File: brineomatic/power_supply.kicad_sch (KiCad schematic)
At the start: 26 parts, among them J8 5.08MM, J9 5.08MM, Q3 20N06, U2 LM74700, U3 XL1509-5.0

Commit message: silkscreen good and all drc errors fixed.
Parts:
- J9: footprint Connector_Phoenix_MSTB:PhoenixContact_MSTBA_2,5_2-G-5,08_1x02_P5.08mm_Horizontal -> yarrboard:PhoenixContact_MSTBA_2,5_2-G-5,08_1x02_P5.08mm_Horizontal
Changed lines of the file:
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@@
 			)
 		)
-		(property "Footprint" "Connector_Phoenix_MSTB:PhoenixContact_MSTBA_2,5_2-G-5,08_1x02_P5.08mm_Horizontal"
+		(property "Footprint" "yarrboard:PhoenixContact_MSTBA_2,5_2-G-5,08_1x02_P5.08mm_Horizontal"
 			(at 46.99 52.07 0)
 			(effects

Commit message: worked on bom for rev b prototype run
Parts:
- C10: value 4.7uF/50v -> 4.7uF / 50v; LCSC C437557 -> (none); now not fitted
- C11: value 10uF/35v -> 10uF / 35v
- C6: LCSC C83170 -> (none)
- C7, C9: LCSC C49678 -> (none)
- C8: value 470nF/50v -> 470nF / 50v; LCSC C106843 -> (none)
- D10, D8: value PWR -> RED; LCSC (none) -> C965799
- D6: LCSC (none) -> C151246
- D7: LCSC (none) -> C148225
- Q3: LCSC (none) -> C36499181
- R18: LCSC C137513 -> (none); now not fitted
- U2: LCSC (none) -> C2941042
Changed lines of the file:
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@@
 			)
 		)
-		(property "Value" "PWR"
+		(property "Value" "RED"
 			(at 143.51 57.4674 90)
 			(effects
@@
 		(property "Sim.Pins" "1=K 2=A"
 			(at 139.7 54.61 0)
+			(effects
+				(font
+					(size 1.27 1.27)
+				)
+				(hide yes)
+			)
+		)
+		(property "LCSC" "C965799"
+			(at 139.7 54.61 90)
 			(effects
 				(font
@@
 			)
 		)
+		(property "LCSC" "C2941042"
+			(at 115.57 62.23 0)
+			(effects
+				(font
+					(size 1.27 1.27)
+				)
+				(hide yes)
+			)
+		)
 		(pin "6"
 		)
@@
 		(in_bom yes)
 		(on_board yes)
-		(dnp no)
+		(dnp yes)
 		(fields_autoplaced yes)
 		(property "Reference" "R18"
@@
 			)
 		)
-		(property "LCSC" "C137513"
+		(property "LCSC" ""
 			(at 118.11 132.08 0)
 			(effects
@@
 			)
 		)
-		(property "LCSC" "C49678"
+		(property "LCSC" ""
 			(at 148.59 128.27 0)
 			(effects
@@
 			)
 		)
+		(property "LCSC" "C36499181"
+			(at 115.57 46.99 90)
+			(effects
+				(font
+					(size 1.27 1.27)
+				)
+				(hide yes)
+			)
+		)
 		(pin "1"
 		)
@@
 			)
 		)
+		(property "LCSC" "C148225"
+			(at 74.93 66.04 90)
+			(effects
+				(font
+					(size 1.27 1.27)
+				)
+				(hide yes)
+			)
+		)
 		(pin "1"
 		)
@@
 			)
 		)
-		(property "LCSC" "C49678"
+		(property "LCSC" ""
 			(at 96.52 58.42 0)
 			(effects
@@
 		(in_bom yes)
 		(on_board yes)
-		(dnp no)
+		(dnp yes)
 		(fields_autoplaced yes)
 		(property "Reference" "C10"
@@
 			)
 		)
-		(property "Value" "4.7uF/50v"
+		(property "Value" "4.7uF / 50v"
 			(at 120.65 125.7363 0)
 			(effects
@@
 			)
 		)
-		(property "LCSC" "C437557"
+		(property "LCSC" ""
 			(at 118.11 124.46 0)
 			(effects
@@
 			)
 		)
+		(property "LCSC" "C151246"
+			(at 74.93 58.42 90)
+			(effects
+				(font
+					(size 1.27 1.27)
+				)
+				(hide yes)
+			)
+		)
 		(pin "1"
 		)
@@
 			)
 		)
-		(property "Value" "PWR"
+		(property "Value" "RED"
 			(at 234.95 127.3174 90)
 			(effects
@@
 			)
 		)
+		(property "LCSC" "C965799"
+			(at 231.14 124.46 90)
+			(effects
+				(font
+					(size 1.27 1.27)
+				)
+				(hide yes)
+			)
+		)
 		(pin "1"
 		)
@@
 			)
 		)
-		(property "LCSC" "C83170"
+		(property "LCSC" ""
 			(at 72.39 128.27 0)
 			(effects
@@
 			)
 		)
-		(property "Value" "10uF/35v"
+		(property "Value" "10uF / 35v"
 			(at 134.62 129.5463 0)
 			(effects
@@
 			)
 		)
-		(property "Value" "470nF/50v"
+		(property "Value" "470nF / 50v"
 			(at 95.25 129.5463 0)
 			(effects
@@
 			)
 		)
-		(property "LCSC" "C106843"
+		(property "LCSC" ""
 			(at 92.71 128.27 0)
 			(effects

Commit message: updated jlc parts rotations and placement offsets
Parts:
- Q3: Position Offset (none) -> -1.778,0.0; Rotation Offset (none) -> 180
- U2: Rotation Offset (none) -> 90
- U3: Rotation Offset (none) -> 180
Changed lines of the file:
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@@
+			)
+		)
+		(property "Rotation Offset" "180"
+			(at 168.91 123.19 0)
+			(effects
+				(font
+					(size 1.27 1.27)
+				)
+				(hide yes)
 			)
 		)
@@
 		)
 		(property "LCSC" "C2941042"
+			(at 115.57 62.23 0)
+			(effects
+				(font
+					(size 1.27 1.27)
+				)
+				(hide yes)
+			)
+		)
+		(property "Rotation Offset" "90"
 			(at 115.57 62.23 0)
 			(effects
@@
 			(at 115.57 46.99 90)
 			(effects
+				(font
+					(size 1.27 1.27)
+				)
+				(hide yes)
+			)
+		)
+		(property "Rotation Offset" "180"
+			(at 115.57 46.99 90)
+			(effects
+				(font
+					(size 1.27 1.27)
+				)
+				(hide yes)
+			)
+		)
+		(property "Position Offset" "-1.778,0.0"
+			(at 115.57 46.99 90)
+			(effects

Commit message: added qwiic i2c connector
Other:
- title: (none) -> https://github.com/hoeken/brineomatic
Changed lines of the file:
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@@
 	(generator_version "9.0")
 	(paper "A4")
+	(title_block
+		(title "https://github.com/hoeken/brineomatic")
+		(date "2025-08-28")
+		(rev "B")
+	)
 	(rectangle
 		(start 21.59 21.59)

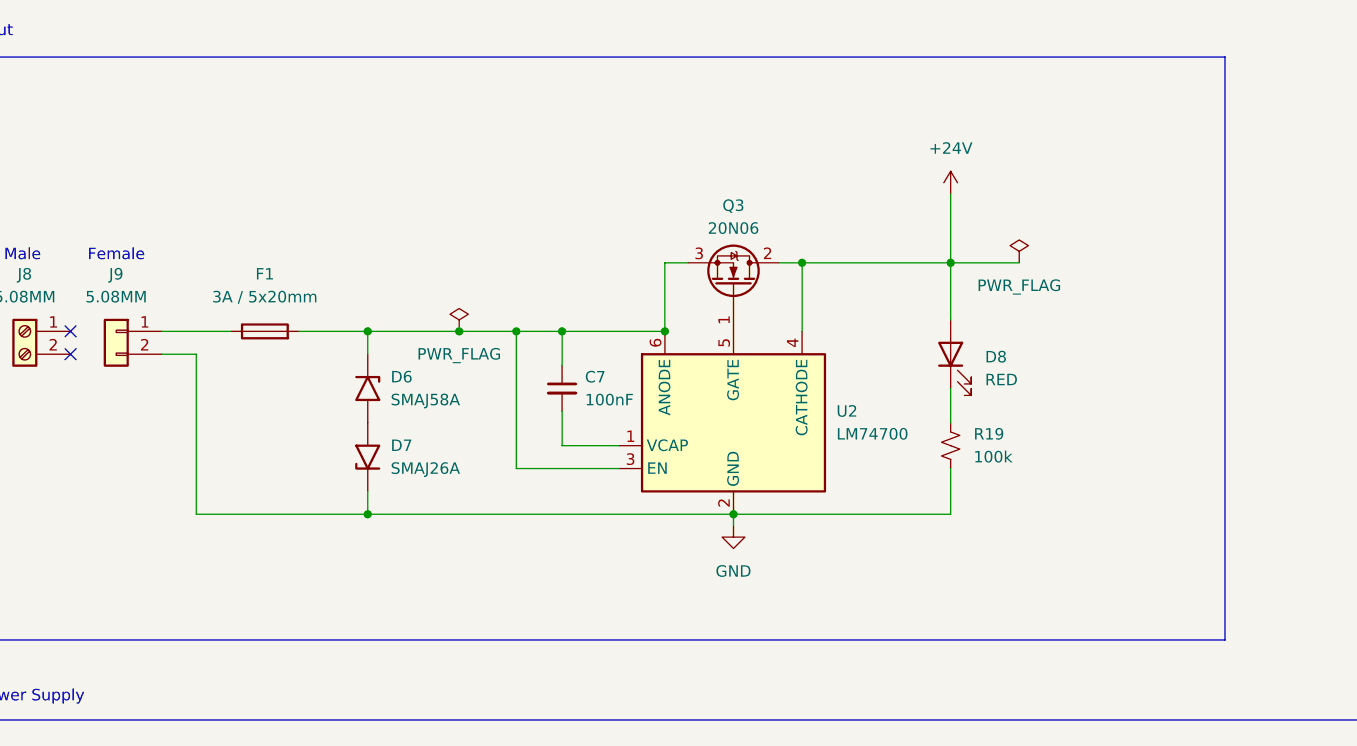
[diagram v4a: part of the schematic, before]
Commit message: added missing cap to reverse polarity protection circuit
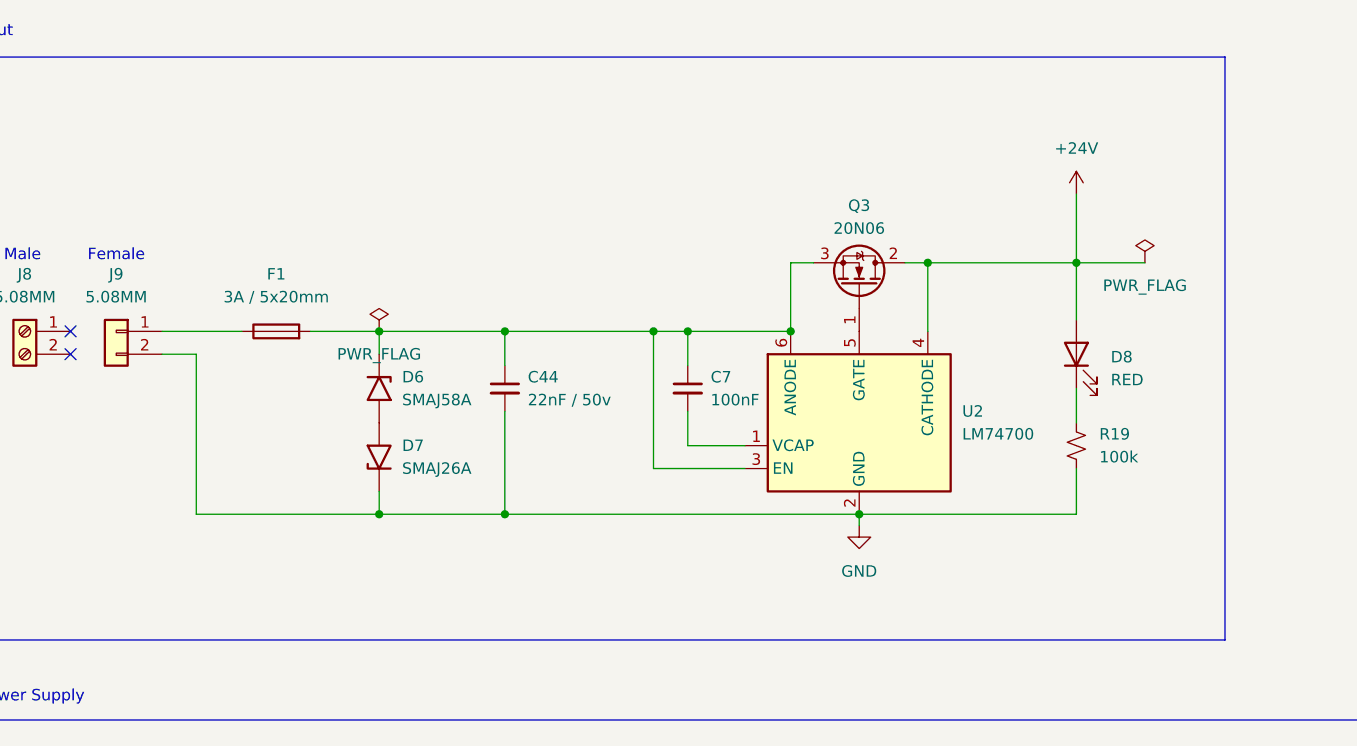
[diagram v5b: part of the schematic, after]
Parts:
- added C44: 22nF / 50v, Capacitor_SMD:C_0603_1608Metric, symbol Device:C_Small
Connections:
- net GND: now also C44.2
- net at C7.1, D6.1 (A1), F1.2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: now also C44.1
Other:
- moved on the sheet: C7, D6, D7, D8, F1, Q3, R19, U2

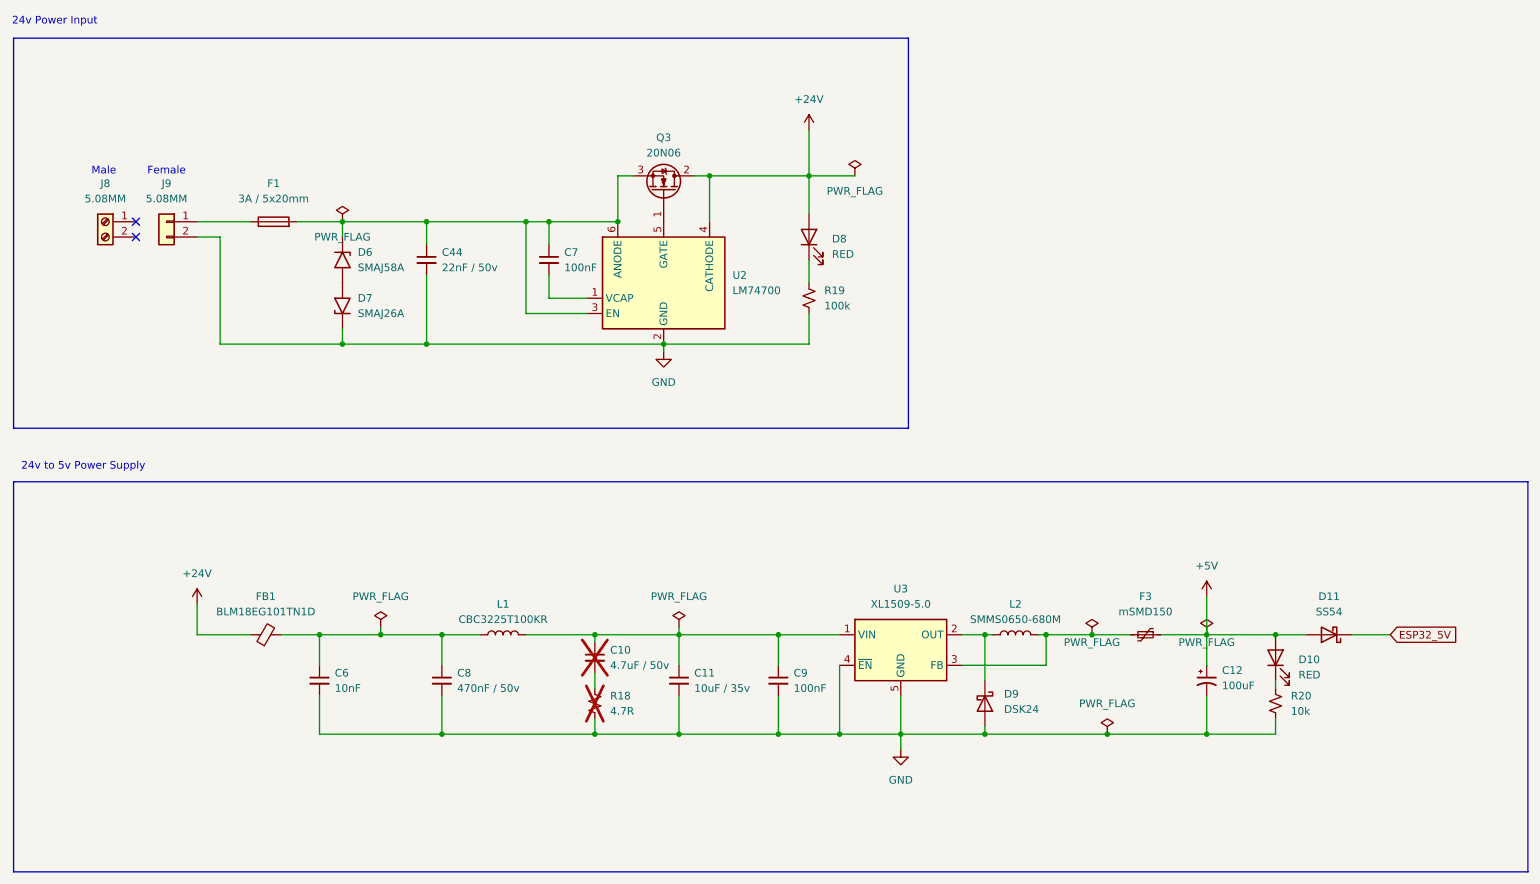
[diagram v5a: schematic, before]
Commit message: added pullup resistor to adc alert
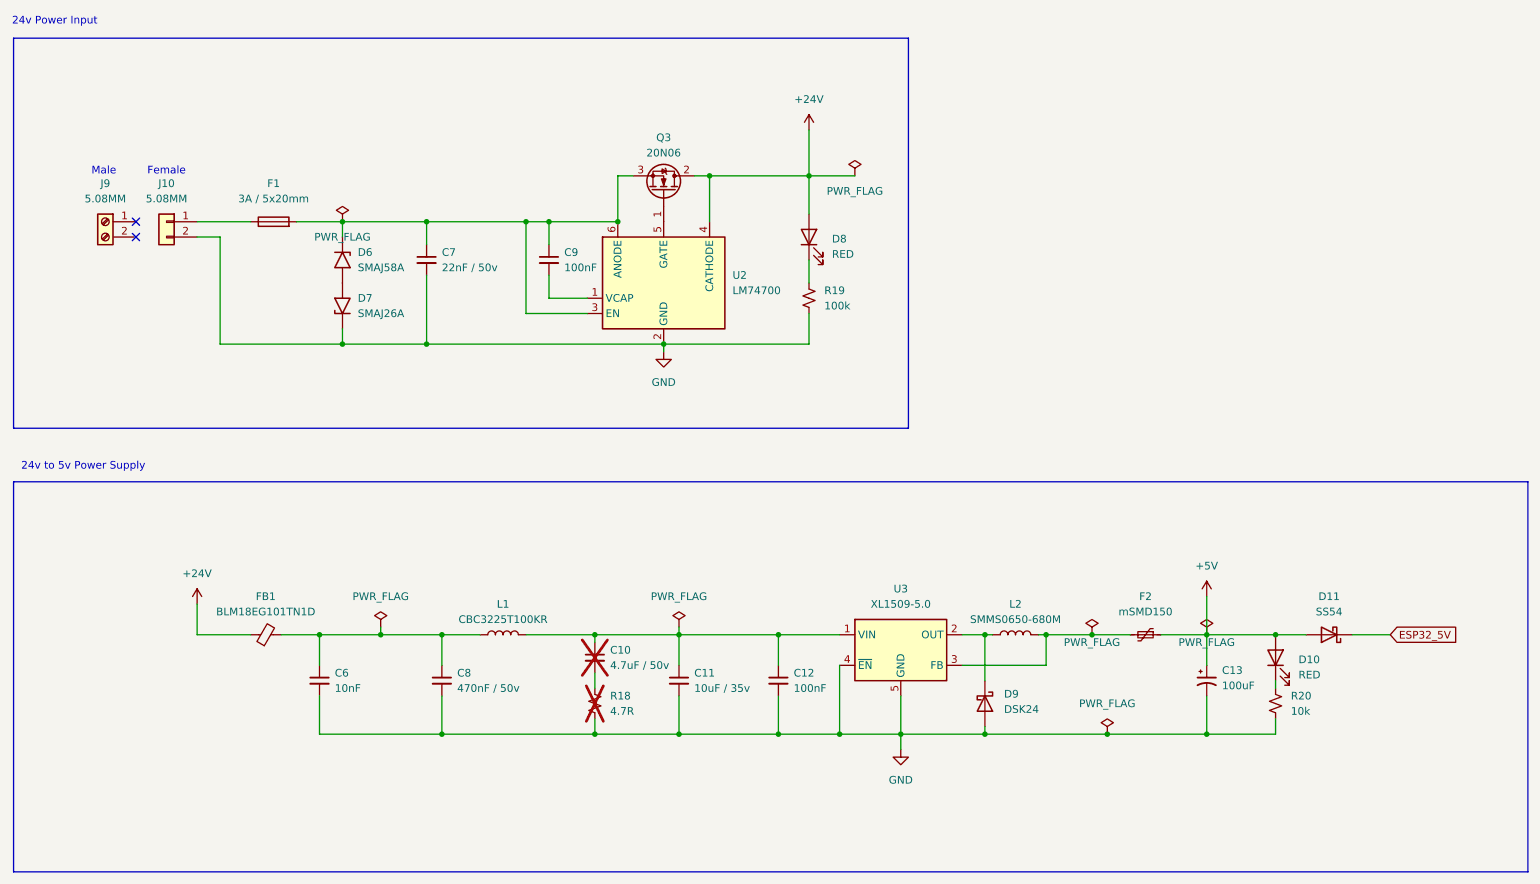
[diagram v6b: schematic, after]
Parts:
- renumbered C9 to C12, C12 to C13, C44 to C7, C7 to C9, F3 to F2, J9 to J10, J8 to J9
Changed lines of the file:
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@@
 		(dnp no)
 		(fields_autoplaced yes)
-		(property "Reference" "#PWR026"
+		(property "Reference" "#PWR028"
 			(at 129.54 80.01 0)
 			(effects
@@
 			(project "brineomatic"
 				(path "/96477ae2-ef08-48f3-8dd4-fe4478541f68/7cbb3b3c-cf93-4880-b816-c6df902b993c"
-					(reference "#PWR026")
+					(reference "#PWR028")
 					(unit 1)
 				)
@@
 		(on_board yes)
 		(dnp no)
-		(property "Reference" "#FLG08"
+		(property "Reference" "#FLG07"
 			(at 219.71 118.745 0)
 			(effects
@@
 			(project "brineomatic"
 				(path "/96477ae2-ef08-48f3-8dd4-fe4478541f68/7cbb3b3c-cf93-4880-b816-c6df902b993c"
-					(reference "#FLG08")
+					(reference "#FLG07")
 					(unit 1)
 				)
@@
 		(dnp no)
 		(fields_autoplaced yes)
-		(property "Reference" "#FLG03"
+		(property "Reference" "#FLG02"
 			(at 82.55 117.475 0)
 			(effects
@@
 			(project "brineomatic"
 				(path "/96477ae2-ef08-48f3-8dd4-fe4478541f68/7cbb3b3c-cf93-4880-b816-c6df902b993c"
-					(reference "#FLG03")
+					(reference "#FLG02")
 					(unit 1)
 				)
@@
 		(dnp no)
 		(fields_autoplaced yes)
-		(property "Reference" "C12"
+		(property "Reference" "C13"
 			(at 222.25 126.5681 0)
 			(effects
@@
 			(project "brineomatic"
 				(path "/96477ae2-ef08-48f3-8dd4-fe4478541f68/7cbb3b3c-cf93-4880-b816-c6df902b993c"
-					(reference "C12")
+					(reference "C13")
 					(unit 1)
 				)
@@
 		(dnp no)
 		(fields_autoplaced yes)
-		(property "Reference" "#PWR029"
+		(property "Reference" "#PWR031"
 			(at 219.71 118.11 0)
 			(effects
@@
 			(project "brineomatic"
 				(path "/96477ae2-ef08-48f3-8dd4-fe4478541f68/7cbb3b3c-cf93-4880-b816-c6df902b993c"
-					(reference "#PWR029")
+					(reference "#PWR031")
 					(unit 1)
 				)
@@
 		(dnp no)
 		(fields_autoplaced yes)
-		(property "Reference" "#FLG07"
+		(property "Reference" "#FLG06"
 			(at 203.2 135.255 0)
 			(effects
@@
 			(project "brineomatic"
 				(path "/96477ae2-ef08-48f3-8dd4-fe4478541f68/7cbb3b3c-cf93-4880-b816-c6df902b993c"
-					(reference "#FLG07")
+					(reference "#FLG06")
 					(unit 1)
 				)
@@
 		(dnp no)
 		(fields_autoplaced yes)
-		(property "Reference" "#FLG04"
+		(property "Reference" "#FLG03"
 			(at 132.08 117.475 0)
 			(effects
@@
 			(project "brineomatic"
 				(path "/96477ae2-ef08-48f3-8dd4-fe4478541f68/7cbb3b3c-cf93-4880-b816-c6df902b993c"
-					(reference "#FLG04")
+					(reference "#FLG03")
 					(unit 1)
 				)
@@
 		(dnp no)
 		(fields_autoplaced yes)
-		(property "Reference" "C9"
+		(property "Reference" "C12"
 			(at 151.13 127.0063 0)
 			(effects
@@
 			(project "brineomatic"
 				(path "/96477ae2-ef08-48f3-8dd4-fe4478541f68/7cbb3b3c-cf93-4880-b816-c6df902b993c"
-					(reference "C9")
+					(reference "C12")
 					(unit 1)
 				)
@@
 		(dnp no)
 		(fields_autoplaced yes)
-		(property "Reference" "F3"
+		(property "Reference" "F2"
 			(at 209.55 114.3 90)
 			(effects
@@
 			(project "brineomatic"
 				(path "/96477ae2-ef08-48f3-8dd4-fe4478541f68/7cbb3b3c-cf93-4880-b816-c6df902b993c"
-					(reference "F3")
+					(reference "F2")
 					(unit 1)
 				)
@@
 		(dnp no)
 		(fields_autoplaced yes)
-		(property "Reference" "#PWR028"
+		(property "Reference" "#PWR030"
 			(at 168.91 146.05 0)
 			(effects
@@
 			(project ""
 				(path "/96477ae2-ef08-48f3-8dd4-fe4478541f68/7cbb3b3c-cf93-4880-b816-c6df902b993c"
-					(reference "#PWR028")
+					(reference "#PWR030")
 					(unit 1)
 				)
@@
 		(on_board yes)
 		(dnp no)
-		(property "Reference" "#FLG06"
+		(property "Reference" "#FLG05"
 			(at 200.66 118.745 0)
 			(effects
@@
 			(project "brineomatic"
 				(path "/96477ae2-ef08-48f3-8dd4-fe4478541f68/7cbb3b3c-cf93-4880-b816-c6df902b993c"
-					(reference "#FLG06")
+					(reference "#FLG05")
 					(unit 1)
 				)
@@
 		(dnp no)
 		(fields_autoplaced yes)
-		(property "Reference" "#PWR027"
+		(property "Reference" "#PWR029"
 			(at 153.67 40.64 0)
 			(effects
@@
 			(project "brineomatic"
 				(path "/96477ae2-ef08-48f3-8dd4-fe4478541f68/7cbb3b3c-cf93-4880-b816-c6df902b993c"
-					(reference "#PWR027")
+					(reference "#PWR029")
 					(unit 1)
 				)
@@
 		(on_board yes)
 		(dnp no)
-		(property "Reference" "C44"
+		(property "Reference" "C7"
 			(at 92.71 57.1563 0)
 			(effects
@@
 			(project "brineomatic"
 				(path "/96477ae2-ef08-48f3-8dd4-fe4478541f68/7cbb3b3c-cf93-4880-b816-c6df902b993c"
-					(reference "C44")
+					(reference "C7")
 					(unit 1)
 				)
@@
 		(on_board yes)
 		(dnp no)
-		(property "Reference" "#FLG05"
+		(property "Reference" "#FLG04"
 			(at 161.29 42.545 0)
 			(effects
@@
 			(project "brineomatic"
 				(path "/96477ae2-ef08-48f3-8dd4-fe4478541f68/7cbb3b3c-cf93-4880-b816-c6df902b993c"
-					(reference "#FLG05")
+					(reference "#FLG04")
 					(unit 1)
 				)
@@
 		(dnp no)
 		(fields_autoplaced yes)
-		(property "Reference" "C7"
+		(property "Reference" "C9"
 			(at 113.03 57.1563 0)
 			(effects
@@
 			(project "brineomatic"
 				(path "/96477ae2-ef08-48f3-8dd4-fe4478541f68/7cbb3b3c-cf93-4880-b816-c6df902b993c"
-					(reference "C7")
+					(reference "C9")
 					(unit 1)
 				)
@@
 		(dnp no)
 		(fields_autoplaced yes)
-		(property "Reference" "J9"
+		(property "Reference" "J10"
 			(at 46.99 45.72 0)
 			(effects
@@
 			(project ""
 				(path "/96477ae2-ef08-48f3-8dd4-fe4478541f68/7cbb3b3c-cf93-4880-b816-c6df902b993c"
-					(reference "J9")
+					(reference "J10")
 					(unit 1)
 				)
@@
 		(dnp no)
 		(fields_autoplaced yes)
-		(property "Reference" "#PWR025"
+		(property "Reference" "#PWR027"
 			(at 52.07 119.38 0)
 			(effects
@@
 			(project "brineomatic"
 				(path "/96477ae2-ef08-48f3-8dd4-fe4478541f68/7cbb3b3c-cf93-4880-b816-c6df902b993c"
-					(reference "#PWR025")
+					(reference "#PWR027")
 					(unit 1)
 				)
@@
 		(on_board no)
 		(dnp no)
-		(property "Reference" "J8"
+		(property "Reference" "J9"
 			(at 36.83 45.72 0)
 			(effects
@@
 			(project ""
 				(path "/96477ae2-ef08-48f3-8dd4-fe4478541f68/7cbb3b3c-cf93-4880-b816-c6df902b993c"
-					(reference "J8")
-					(unit 1)
-				)
+					(reference "J9")
+					(unit 1)
+				)
